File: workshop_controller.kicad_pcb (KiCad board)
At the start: 4 copper layers, 184.9 x 88 mm, 66 parts, among them J1 Conn_02x10_Odd_Even, J2 Conn_02x10_Odd_Even, J3 AudioJack3, J4 Micro_SD_Card, J5 Conn_02x25_Odd_Even, J6 Conn_01x05_Female, J7 LOGO_TOUCH, M1 Microphone4, SW1 SW_Push, SW2 SW_Push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

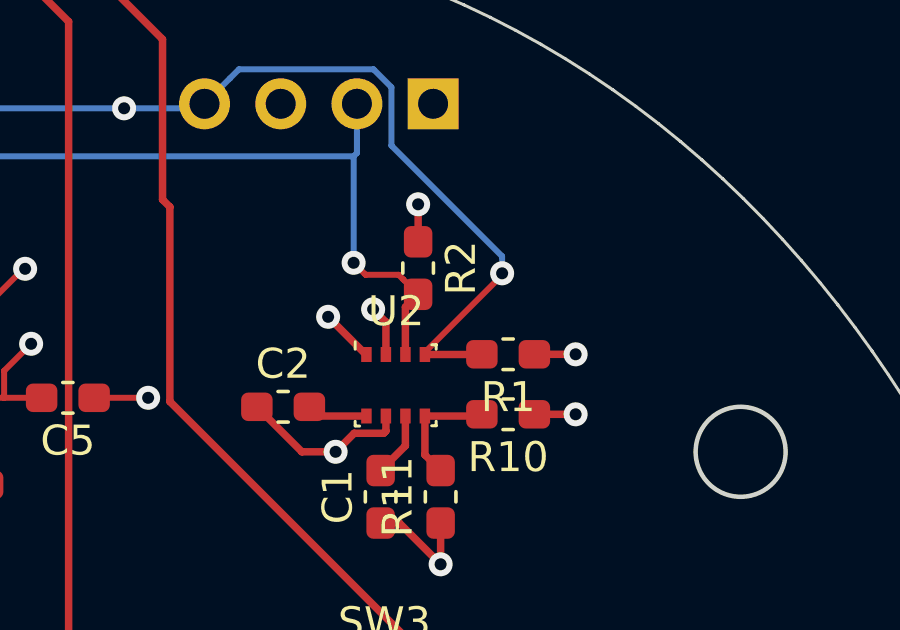
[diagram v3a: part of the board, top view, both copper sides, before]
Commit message: Swap resistors
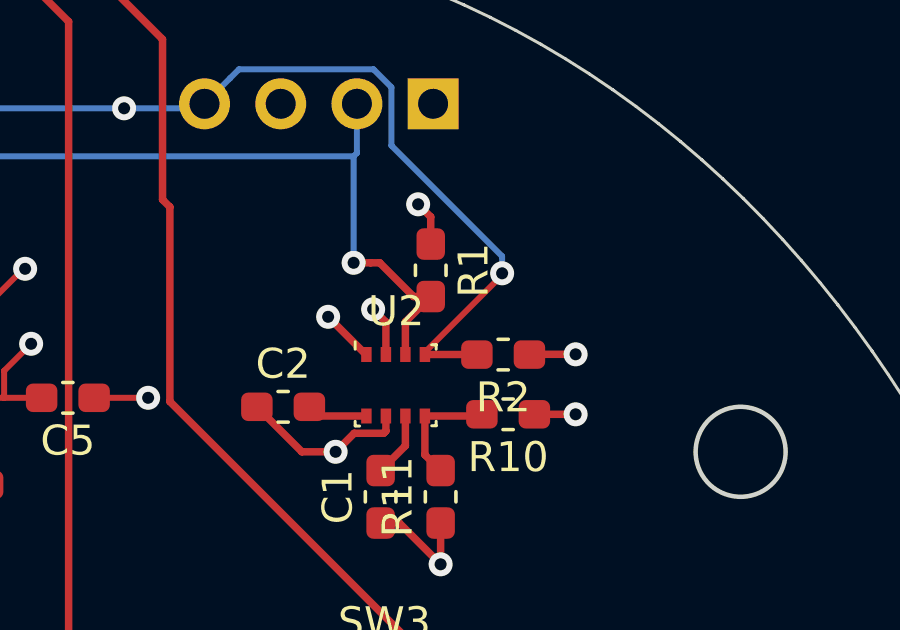
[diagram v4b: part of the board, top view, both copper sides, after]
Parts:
- moved R2 4.04 mm to (226.0, 67.7), turned to 180 degrees
- moved R1 3.81 mm to (223.6, 64.8), turned to 270 degrees
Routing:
- net /I2C_SDA: track 145.0 -> 145.6 mm
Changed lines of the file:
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@@
     (thickness 1.6)
     (drawings 305)
-    (tracks 756)
+    (tracks 757)
     (zones 0)
     (modules 66)
@@
     (add_net "Net-(U5-Pad7)")
   )
+  (module Resistor_SMD:R_0603_1608Metric_Pad1.05x0.95mm_HandSolder (layer F.Cu)
+    (at 223.57 64.85 270)
+    (descr "Resistor SMD 0603 (1608 Metric), square (rectangular) end terminal, IPC_7351 nominal with elongated pad for handsoldering. (Body size source: http://www.tortai-tech.com/upload/download/2011102023233369053.pdf), generated with kicad-footprint-generator")
+    (tags "resistor handsolder")
+    (attr smd)
+    (fp_text reference R1 (at 0 -1.43 270) (layer F.SilkS)
+      (effects (font (size 1 1) (thickness 0.15)))
+    )
+    (fp_text value 4.7kΩ (at 0 1.43 270) (layer F.Fab)
+      (effects (font (size 1 1) (thickness 0.15)))
+    )
+    (fp_line (start -0.8 0.4) (end -0.8 -0.4) (layer F.Fab) (width 0.1))
+    (fp_line (start -0.8 -0.4) (end 0.8 -0.4) (layer F.Fab) (width 0.1))
+    (fp_line (start 0.8 -0.4) (end 0.8 0.4) (layer F.Fab) (width 0.1))
+    (fp_line (start 0.8 0.4) (end -0.8 0.4) (layer F.Fab) (width 0.1))
+    (fp_line (start -0.171267 -0.51) (end 0.171267 -0.51) (layer F.SilkS) (width 0.12))
+    (fp_line (start -0.171267 0.51) (end 0.171267 0.51) (layer F.SilkS) (width 0.12))
+    (fp_line (start -1.65 0.73) (end -1.65 -0.73) (layer F.CrtYd) (width 0.05))
+    (fp_line (start -1.65 -0.73) (end 1.65 -0.73) (layer F.CrtYd) (width 0.05))
+    (fp_line (start 1.65 -0.73) (end 1.65 0.73) (layer F.CrtYd) (width 0.05))
+    (fp_line (start 1.65 0.73) (end -1.65 0.73) (layer F.CrtYd) (width 0.05))
+    (fp_text user %R (at 0 0 270) (layer F.Fab)
+      (effects (font (size 0.4 0.4) (thickness 0.06)))
+    )
+    (pad 1 smd roundrect (at -0.875 0 270) (size 1.05 0.95) (layers F.Cu F.Paste F.Mask) (roundrect_rratio 0.25)
+      (net 22 +3V3))
+    (pad 2 smd roundrect (at 0.875 0 270) (size 1.05 0.95) (layers F.Cu F.Paste F.Mask) (roundrect_rratio 0.25)
+      (net 63 /I2C_SDA))
+    (model ${KISYS3DMOD}/Resistor_SMD.3dshapes/R_0603_1608Metric.wrl
+      (at (xyz 0 0 0))
+      (scale (xyz 1 1 1))
+      (rotate (xyz 0 0 0))
+    )
+  )
   (module svg2mod (layer F.Cu)
     (at 0 0)
@@
   )
   (module Resistor_SMD:R_0603_1608Metric_Pad1.05x0.95mm_HandSolder (layer F.Cu)
-    (at 226.15 67.65 180)
+    (at 225.985 67.66 180)
     (descr "Resistor SMD 0603 (1608 Metric), square (rectangular) end terminal, IPC_7351 nominal with elongated pad for handsoldering. (Body size source: http://www.tortai-tech.com/upload/download/2011102023233369053.pdf), generated with kicad-footprint-generator")
     (tags "resistor handsolder")
     (attr smd)
-    (fp_text reference R1 (at 0 -1.43 180) (layer F.SilkS)
+    (fp_text reference R2 (at 0 -1.43 180) (layer F.SilkS)
       (effects (font (size 1 1) (thickness 0.15)))
     )
@@
       (effects (font (size 1 1) (thickness 0.15)))
     )
-    (fp_line (start -0.8 0.4) (end -0.8 -0.4) (layer F.Fab) (width 0.1))
-    (fp_line (start -0.8 -0.4) (end 0.8 -0.4) (layer F.Fab) (width 0.1))
-    (fp_line (start 0.8 -0.4) (end 0.8 0.4) (layer F.Fab) (width 0.1))
-    (fp_line (start 0.8 0.4) (end -0.8 0.4) (layer F.Fab) (width 0.1))
-    (fp_line (start -0.171267 -0.51) (end 0.171267 -0.51) (layer F.SilkS) (width 0.12))
-    (fp_line (start -0.171267 0.51) (end 0.171267 0.51) (layer F.SilkS) (width 0.12))
-    (fp_line (start -1.65 0.73) (end -1.65 -0.73) (layer F.CrtYd) (width 0.05))
-    (fp_line (start -1.65 -0.73) (end 1.65 -0.73) (layer F.CrtYd) (width 0.05))
-    (fp_line (start 1.65 -0.73) (end 1.65 0.73) (layer F.CrtYd) (width 0.05))
-    (fp_line (start 1.65 0.73) (end -1.65 0.73) (layer F.CrtYd) (width 0.05))
     (fp_text user %R (at 0 0 180) (layer F.Fab)
       (effects (font (size 0.4 0.4) (thickness 0.06)))
     )
-    (pad 1 smd roundrect (at -0.875 0 180) (size 1.05 0.95) (layers F.Cu F.Paste F.Mask) (roundrect_rratio 0.25)
-      (net 22 +3V3))
-    (pad 2 smd roundrect (at 0.875 0 180) (size 1.05 0.95) (layers F.Cu F.Paste F.Mask) (roundrect_rratio 0.25)
-      (net 63 /I2C_SDA))
-    (model ${KISYS3DMOD}/Resistor_SMD.3dshapes/R_0603_1608Metric.wrl
-      (at (xyz 0 0 0))
-      (scale (xyz 1 1 1))
-      (rotate (xyz 0 0 0))
-    )
-  )
-  (module Resistor_SMD:R_0603_1608Metric_Pad1.05x0.95mm_HandSolder (layer F.Cu)
-    (at 223.15 64.775 270)
-    (descr "Resistor SMD 0603 (1608 Metric), square (rectangular) end terminal, IPC_7351 nominal with elongated pad for handsoldering. (Body size source: http://www.tortai-tech.com/upload/download/2011102023233369053.pdf), generated with kicad-footprint-generator")
-    (tags "resistor handsolder")
-    (attr smd)
-    (fp_text reference R2 (at 0 -1.43 270) (layer F.SilkS)
-      (effects (font (size 1 1) (thickness 0.15)))
-    )
-    (fp_text value 4.7kΩ (at 0 1.43 270) (layer F.Fab)
-      (effects (font (size 1 1) (thickness 0.15)))
-    )
-    (fp_text user %R (at 0 0 270) (layer F.Fab)
-      (effects (font (size 0.4 0.4) (thickness 0.06)))
-    )
     (fp_line (start 1.65 0.73) (end -1.65 0.73) (layer F.CrtYd) (width 0.05))
     (fp_line (start 1.65 -0.73) (end 1.65 0.73) (layer F.CrtYd) (width 0.05))
@@
     (fp_line (start -0.8 -0.4) (end 0.8 -0.4) (layer F.Fab) (width 0.1))
     (fp_line (start -0.8 0.4) (end -0.8 -0.4) (layer F.Fab) (width 0.1))
-    (pad 2 smd roundrect (at 0.875 0 270) (size 1.05 0.95) (layers F.Cu F.Paste F.Mask) (roundrect_rratio 0.25)
+    (pad 2 smd roundrect (at 0.875 0 180) (size 1.05 0.95) (layers F.Cu F.Paste F.Mask) (roundrect_rratio 0.25)
       (net 62 /I2C_SCK))
-    (pad 1 smd roundrect (at -0.875 0 270) (size 1.05 0.95) (layers F.Cu F.Paste F.Mask) (roundrect_rratio 0.25)
+    (pad 1 smd roundrect (at -0.875 0 180) (size 1.05 0.95) (layers F.Cu F.Paste F.Mask) (roundrect_rratio 0.25)
       (net 22 +3V3))
     (model ${KISYS3DMOD}/Resistor_SMD.3dshapes/R_0603_1608Metric.wrl
@@
   (via (at 228.4 67.65) (size 0.8) (drill 0.4) (layers F.Cu B.Cu) (net 22))
   (via (at 223.15 62.65) (size 0.8) (drill 0.4) (layers F.Cu B.Cu) (net 22))
-  (segment (start 223.15 63.9) (end 223.15 62.65) (width 0.25) (layer F.Cu) (net 22))
   (via (at 221.65 66.15) (size 0.8) (drill 0.4) (layers F.Cu B.Cu) (net 22))
   (segment (start 222.076 67.657) (end 222.076 66.576) (width 0.25) (layer F.Cu) (net 22))
@@
   (segment (start 196.25 65.075) (end 198.135 65.075) (width 0.25) (layer F.Cu) (net 22))
   (segment (start 198.135 65.075) (end 198.64 65.58) (width 0.25) (layer F.Cu) (net 22))
+  (segment (start 223.57 63.07) (end 223.15 62.65) (width 0.25) (layer F.Cu) (net 22))
+  (segment (start 223.57 63.975) (end 223.57 63.07) (width 0.25) (layer F.Cu) (net 22))
   (segment (start 188.949072 64.575928) (end 188.45 65.075) (width 0.25) (layer F.Cu) (net 26))
   (segment (start 190.850928 64.575928) (end 188.949072 64.575928) (width 0.25) (layer F.Cu) (net 26))
@@
   (segment (start 141.006998 100.33) (end 133.274999 92.598001) (width 0.25) (layer F.Cu) (net 62))
   (segment (start 146.15 100.33) (end 141.006998 100.33) (width 0.25) (layer F.Cu) (net 62))
-  (segment (start 222.726 66.074) (end 223.15 65.65) (width 0.25) (layer F.Cu) (net 63))
-  (segment (start 222.726 67.657) (end 222.726 66.074) (width 0.25) (layer F.Cu) (net 63))
   (segment (start 141.574999 79.905001) (end 152.894999 79.905001) (width 0.25) (layer B.Cu) (net 63))
   (segment (start 140.21 81.27) (end 141.574999 79.905001) (width 0.25) (layer B.Cu) (net 63))
@@
   (via (at 221 64.6) (size 0.8) (drill 0.4) (layers F.Cu B.Cu) (net 63))
   (segment (start 221 61.05) (end 221 64.6) (width 0.2) (layer B.Cu) (net 63))
-  (segment (start 222.650928 65.150928) (end 223.15 65.65) (width 0.2) (layer F.Cu) (net 63))
-  (segment (start 222.499999 64.999999) (end 222.650928 65.150928) (width 0.2) (layer F.Cu) (net 63))
-  (segment (start 221.399999 64.999999) (end 222.499999 64.999999) (width 0.2) (layer F.Cu) (net 63))
-  (segment (start 221 64.6) (end 221.399999 64.999999) (width 0.2) (layer F.Cu) (net 63))
   (via (at 144.78 109.22) (size 0.8) (drill 0.4) (layers F.Cu B.Cu) (net 63))
   (segment (start 145.7 107.05) (end 145.7 108.3) (width 0.25) (layer F.Cu) (net 63))
@@
   (segment (start 139.71 81.27) (end 140.21 81.27) (width 0.25) (layer F.Cu) (net 63))
   (segment (start 137.16 83.82) (end 139.71 81.27) (width 0.25) (layer F.Cu) (net 63))
+  (segment (start 221.565685 64.6) (end 221 64.6) (width 0.25) (layer F.Cu) (net 63))
+  (segment (start 221.87 64.6) (end 221.565685 64.6) (width 0.25) (layer F.Cu) (net 63))
+  (segment (start 222.995 65.725) (end 221.87 64.6) (width 0.25) (layer F.Cu) (net 63))
+  (segment (start 223.57 65.725) (end 222.995 65.725) (width 0.25) (layer F.Cu) (net 63))
+  (segment (start 222.726 66.569) (end 222.726 67.657) (width 0.25) (layer F.Cu) (net 63))
+  (segment (start 223.57 65.725) (end 222.726 66.569) (width 0.25) (layer F.Cu) (net 63))
   (segment (start 222.726 70.699) (end 221.9 71.525) (width 0.25) (layer F.Cu) (net 64))
   (segment (start 222.726 69.707) (end 222.726 70.699) (width 0.25) (layer F.Cu) (net 64))

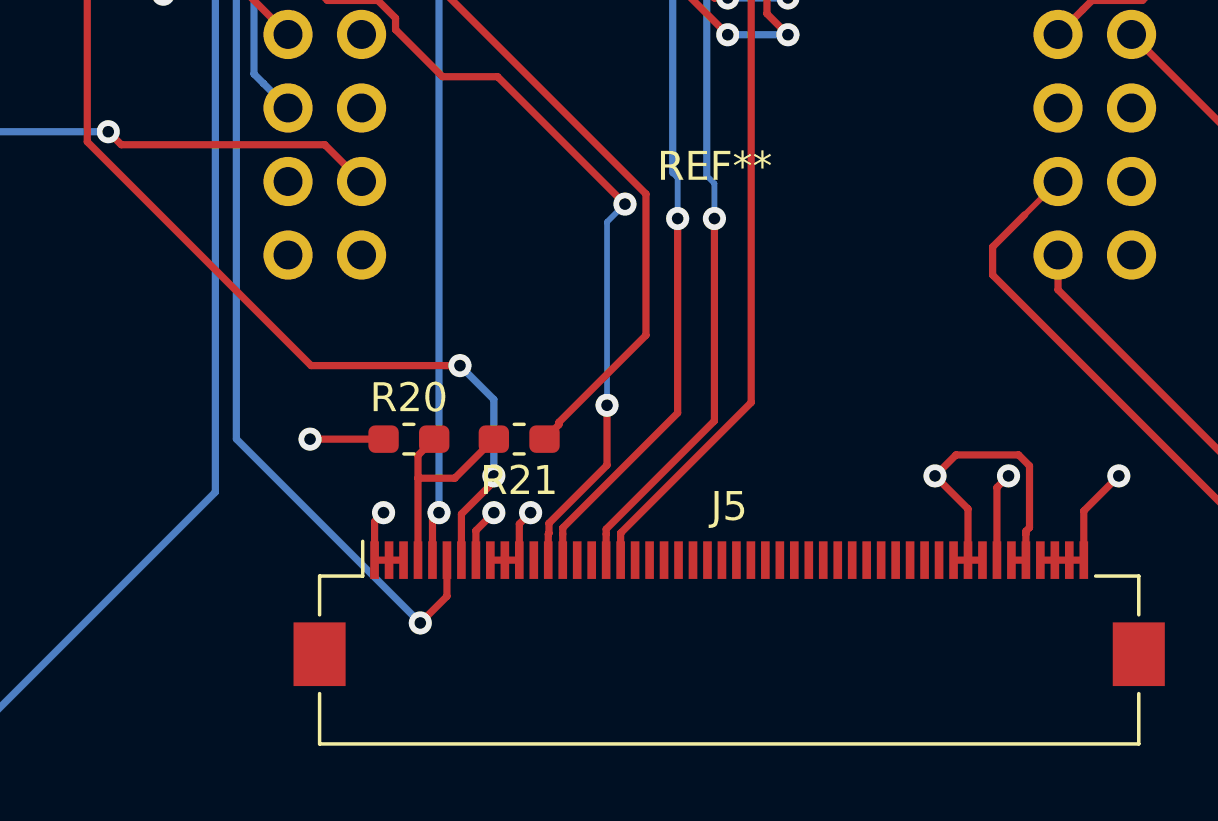
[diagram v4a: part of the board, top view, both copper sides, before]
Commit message: Fix display circuit
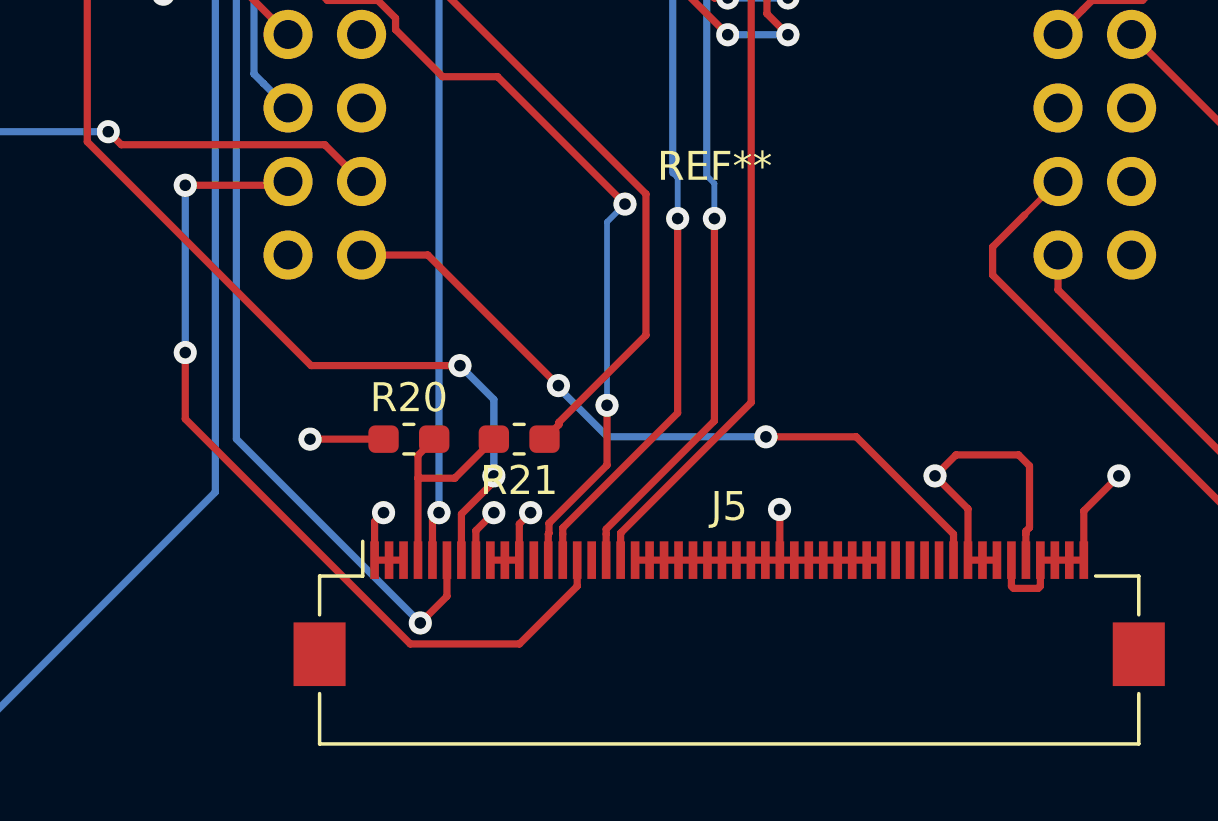
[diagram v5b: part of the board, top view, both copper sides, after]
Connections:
- net /PIN_CLK renamed /PIN_CLK_06
- net Net-(J2-Pad1) renamed /PIN_TXD
- J2 pad 18: /PIN_SD1 -> /PIN_SD1_08
- J2 pad 19: /PIN_SDO -> /PIN_SDO_07
- J5 pad 15: Net-(J5-Pad15) -> /PIN_SD1_08
- J5 pad 19: Net-(J5-Pad19) -> GND
- J5 pad 20: Net-(J5-Pad20) -> GND
- J5 pad 21: Net-(J5-Pad21) -> GND
- J5 pad 22: Net-(J5-Pad22) -> GND
- J5 pad 23: Net-(J5-Pad23) -> GND
- J5 pad 24: Net-(J5-Pad24) -> GND
- J5 pad 25: Net-(J5-Pad25) -> GND
- J5 pad 26: Net-(J5-Pad26) -> GND
- J5 pad 27: Net-(J5-Pad27) -> GND
- J5 pad 28: Net-(J5-Pad28) -> GND
- J5 pad 29: Net-(J5-Pad29) -> GND
- J5 pad 30: Net-(J5-Pad30) -> GND
- J5 pad 31: Net-(J5-Pad31) -> GND
- J5 pad 32: Net-(J5-Pad32) -> GND
- J5 pad 33: Net-(J5-Pad33) -> GND
- J5 pad 34: Net-(J5-Pad34) -> GND
- J5 pad 35: Net-(J5-Pad35) -> GND
- J5 pad 36: Net-(J5-Pad36) -> GND
- J5 pad 41: +3V3 -> /PIN_SDO_07
- J5 pad 44: GND -> +3V3
- J5 pad 45: +3V3 -> GND
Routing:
- net /PIN_SD1_08: track 0.00 -> 30.2 mm, vias 0 -> 2
- net /PIN_SDO_07: track 0.00 -> 25.4 mm, vias 0 -> 2
- net GND: track 123.6 -> 133.6 mm
- net +3V3: track 102.4 -> 101.9 mm

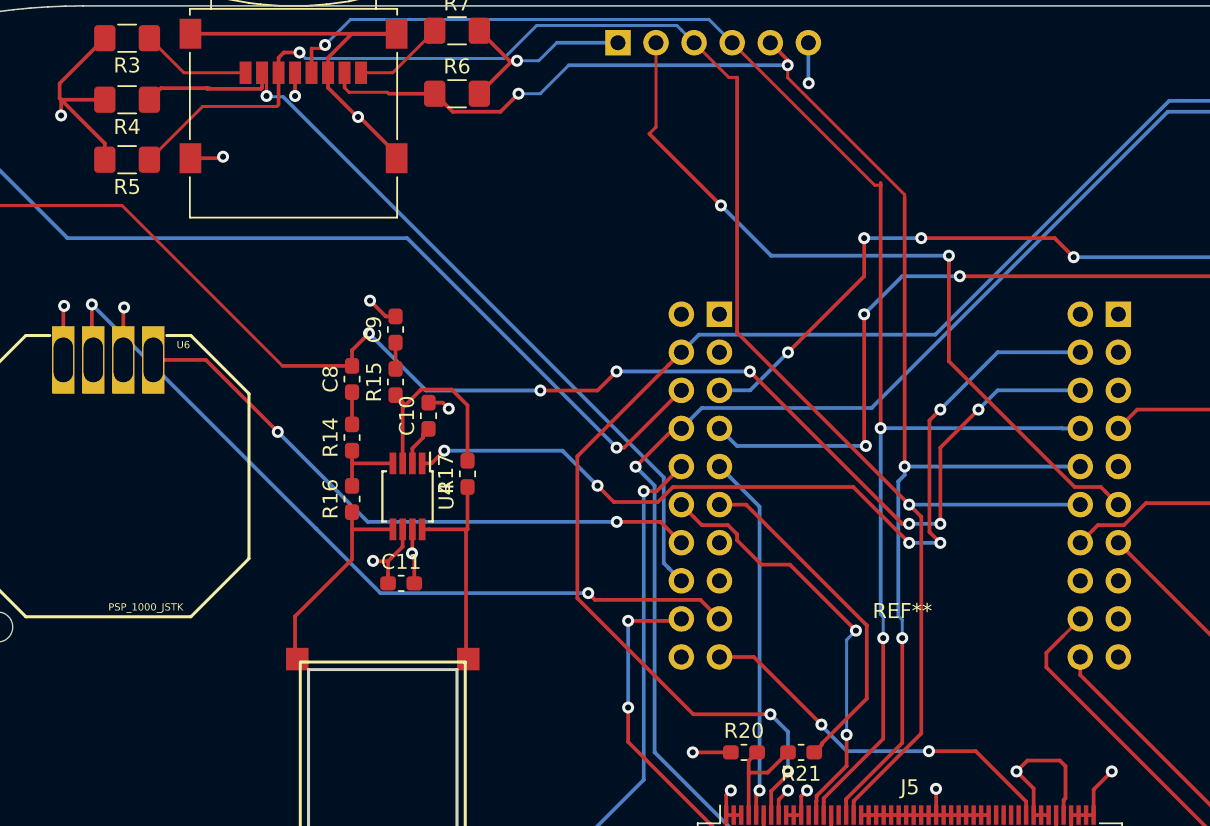
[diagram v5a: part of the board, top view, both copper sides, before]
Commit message: Do design rules check
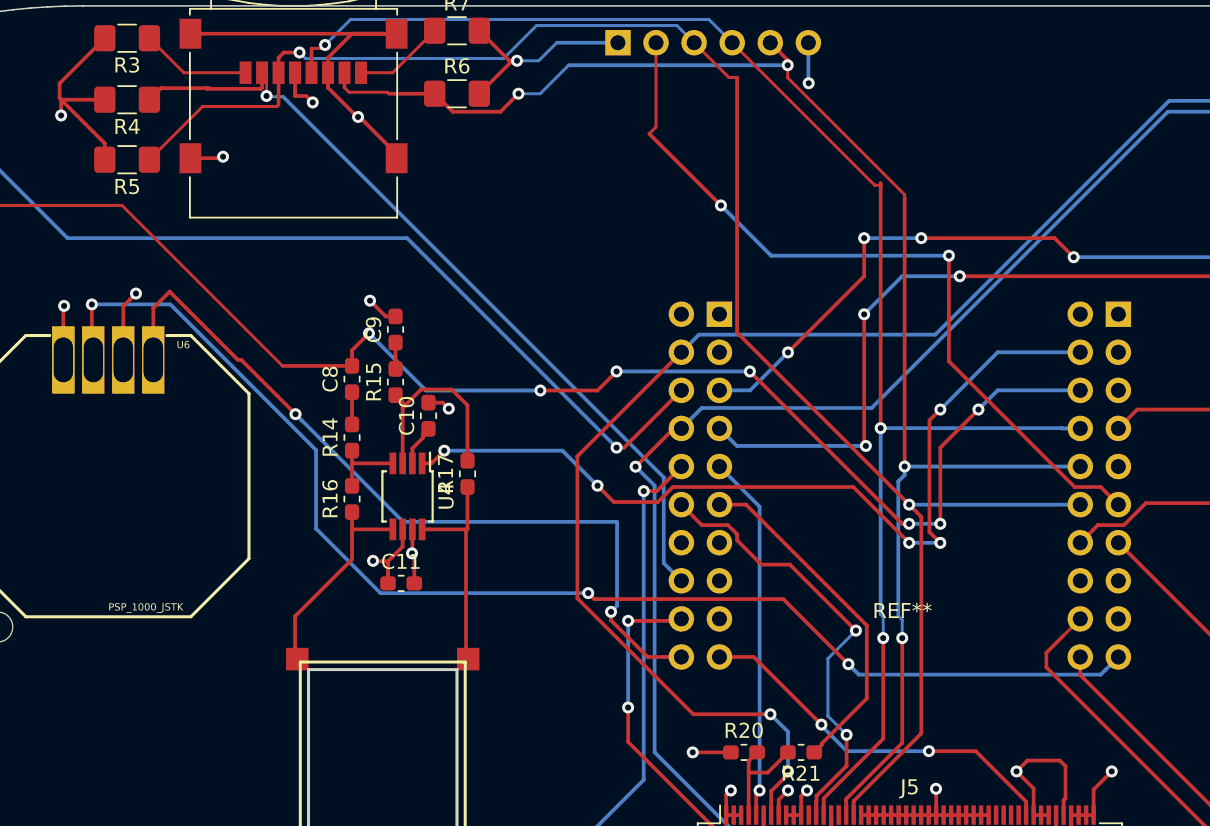
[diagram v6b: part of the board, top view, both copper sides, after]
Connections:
- net /PIN_SD2 renamed /PIN_SD2_09
- J1 pad 19: /PIN_CMD -> /JOY_Y
- J2 pad 14: /JOY_X -> /PIN_0
- J2 pad 17: /JOY_Y -> /PIN_TDO_15
- J2 pad 20: /PIN_CLK_06 -> /JOY_X
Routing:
- net /JOY_Y: track 54.3 -> 86.0 mm, vias 2 -> 3
- net /JOY_X: track 40.3 -> 53.6 mm
- net +3V3: track 101.9 -> 104.5 mm
- net /PIN_4: track 28.8 -> 29.8 mm
